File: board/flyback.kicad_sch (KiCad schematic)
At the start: 25 parts, among them U1 MP8007, U2 POE30P-50L

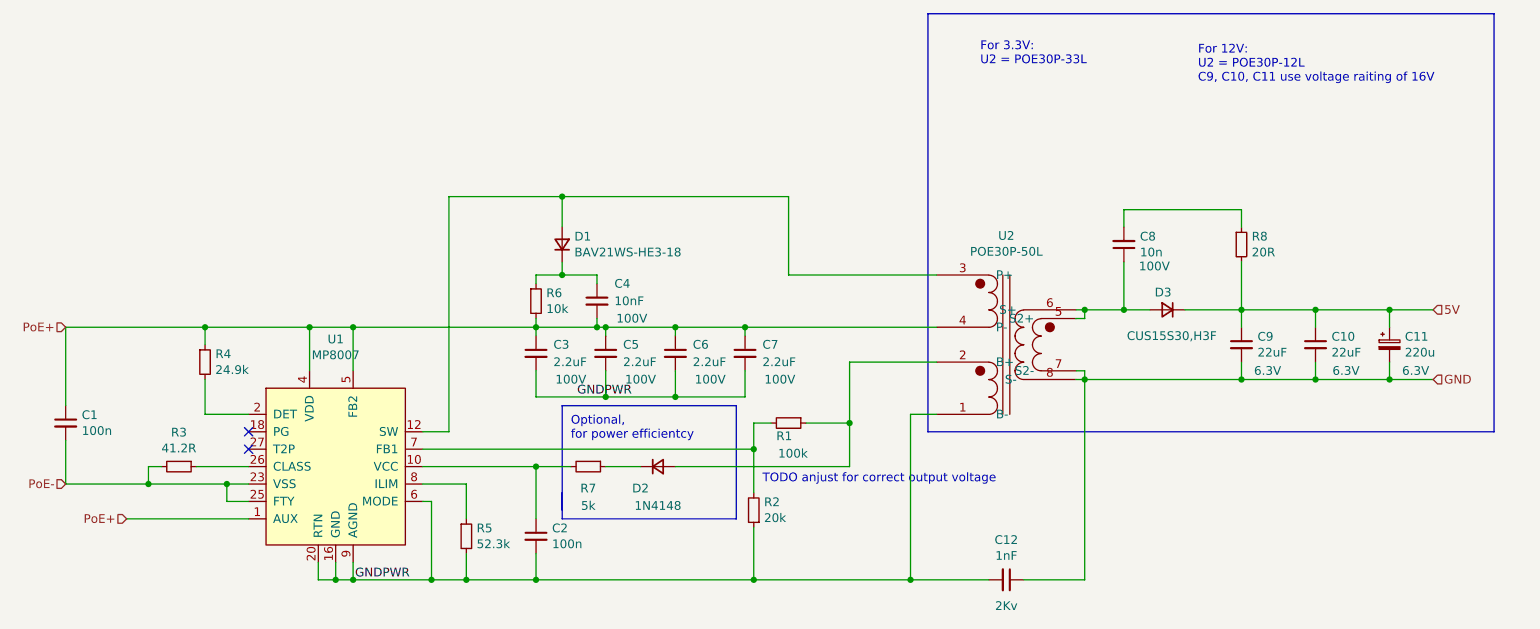
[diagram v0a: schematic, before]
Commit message: updated current limmit resistor
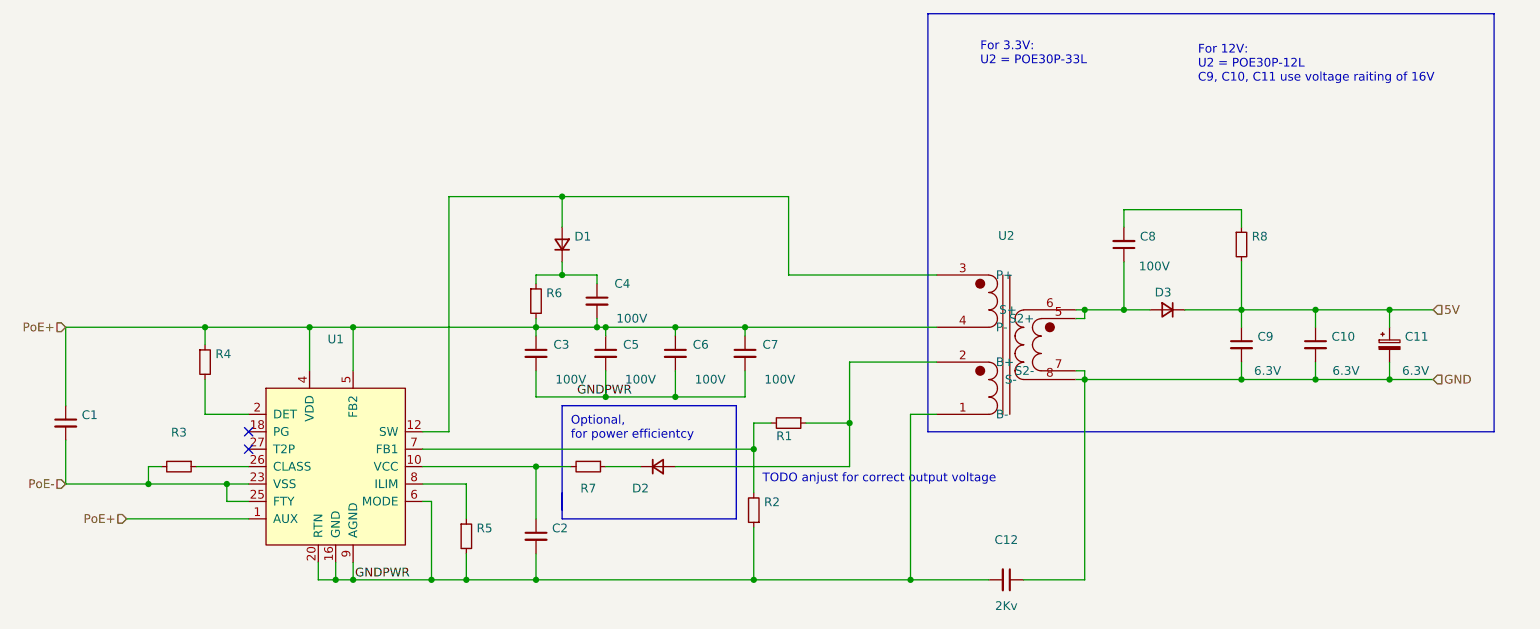
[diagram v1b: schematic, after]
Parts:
- C1, C2: value 100n -> (none); footprint Capacitor_SMD:C_0603_1608Metric -> (none)
- C10, C9: value 22uF -> (none); footprint Capacitor_SMD:C_0805_2012Metric -> (none)
- C11: value 220u -> (none); footprint Capacitor_Tantalum_SMD:CP_EIA-7343-31_Kemet-D -> (none)
- C12: value 1nF -> (none); footprint Capacitor_SMD:C_1806_4516Metric -> (none)
- C3, C5, C6, C7: value 2.2uF -> (none); footprint Capacitor_SMD:C_1210_3225Metric -> (none)
- C4: value 10nF -> (none); footprint Capacitor_SMD:C_0603_1608Metric -> (none)
- C8: value 10n -> (none); footprint Capacitor_SMD:C_0603_1608Metric -> (none)
- D1: value BAV21WS-HE3-18 -> (none); footprint Diode_SMD:D_SOD-323_HandSoldering -> (none)
- D2: value 1N4148 -> (none); footprint Diode_SMD:D_SOD-323_HandSoldering -> (none)
- D3: value CUS15S30,H3F -> (none); footprint Diode_SMD:D_SOD-323_HandSoldering -> (none)
- R1: value 100k -> (none); footprint Resistor_SMD:R_0603_1608Metric -> (none)
- R2: value 20k -> (none); footprint Resistor_SMD:R_0603_1608Metric -> (none)
- R3: value 41.2R -> (none); footprint Resistor_SMD:R_0603_1608Metric -> (none)
- R4: value 24.9k -> (none); footprint Resistor_SMD:R_0603_1608Metric -> (none)
- R5: value 52.3k -> (none); footprint Resistor_SMD:R_0603_1608Metric -> (none)
- R6: value 10k -> (none); footprint Resistor_SMD:R_0603_1608Metric -> (none)
- R7: value 5k -> (none); footprint Resistor_SMD:R_0603_1608Metric -> (none)
- R8: value 20R -> (none); footprint Resistor_SMD:R_0603_1608Metric -> (none)
- U1: value MP8007 -> (none); footprint Package_DFN_QFN:QFN-28-1EP_4x5mm_P0.5mm_EP2.65x3.65mm_ThermalVias -> (none)
- U2: value POE30P-50L -> (none); footprint b033:Transformer_Coilcraft_POE30P -> (none)
